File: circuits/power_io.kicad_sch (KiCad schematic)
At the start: 19 parts, among them J3 AD7606 out, J4 LASER+MPD out, J5 LASER PSU, J6 EXT 5V

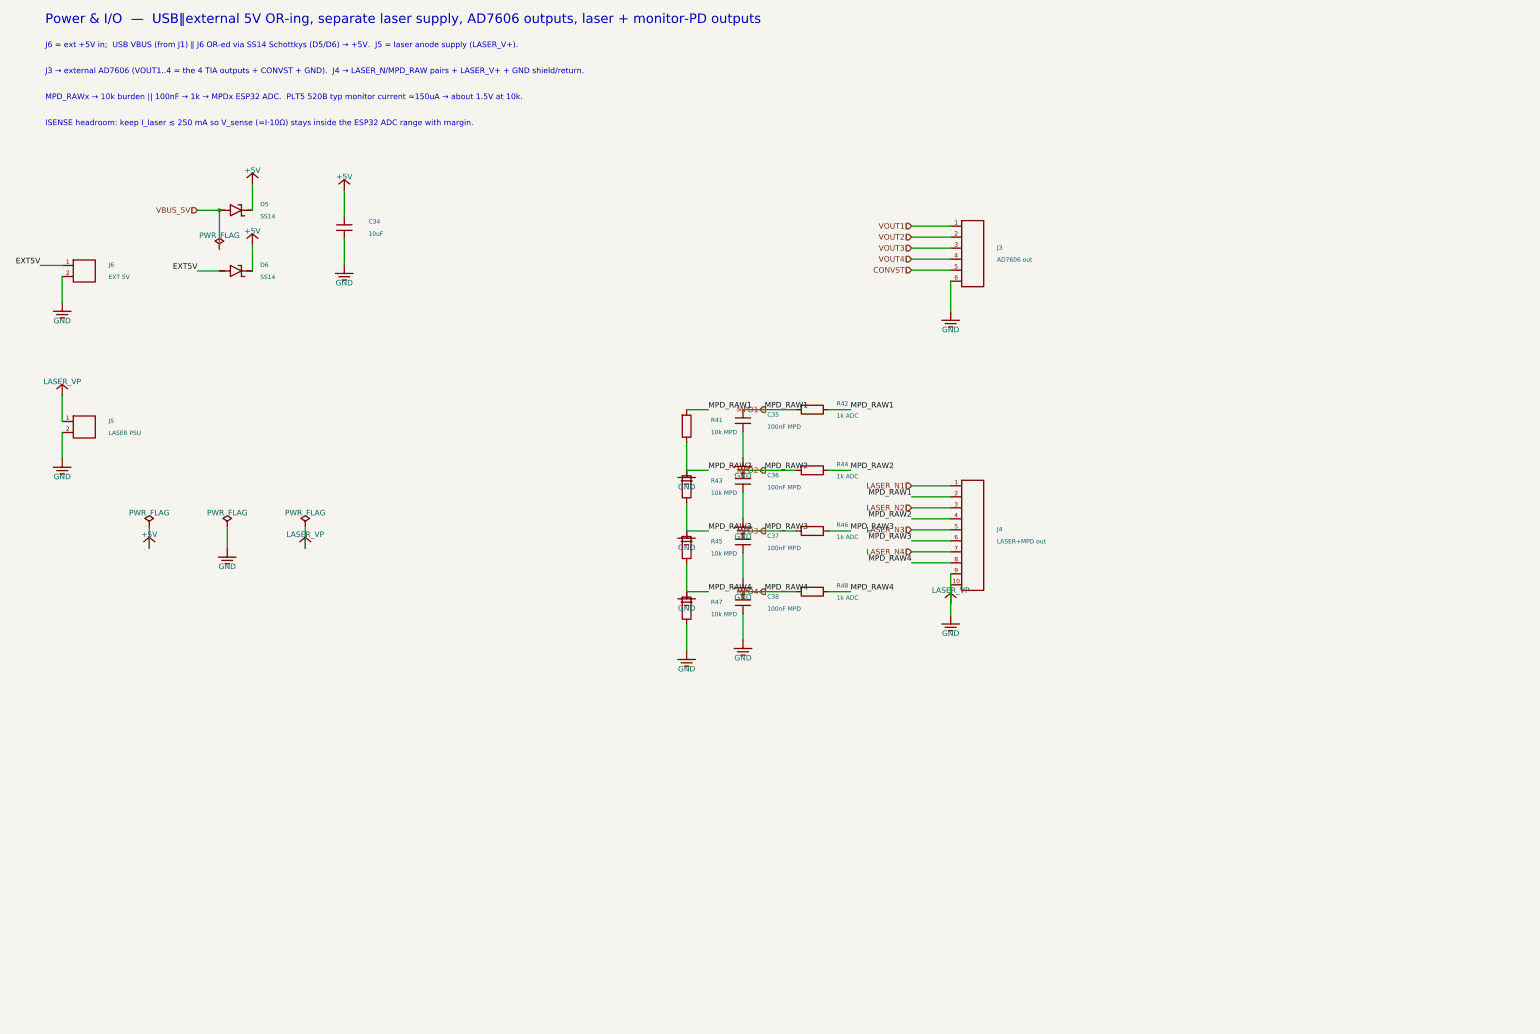
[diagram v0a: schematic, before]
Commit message: chore(circuits): update laser controller release artifacts
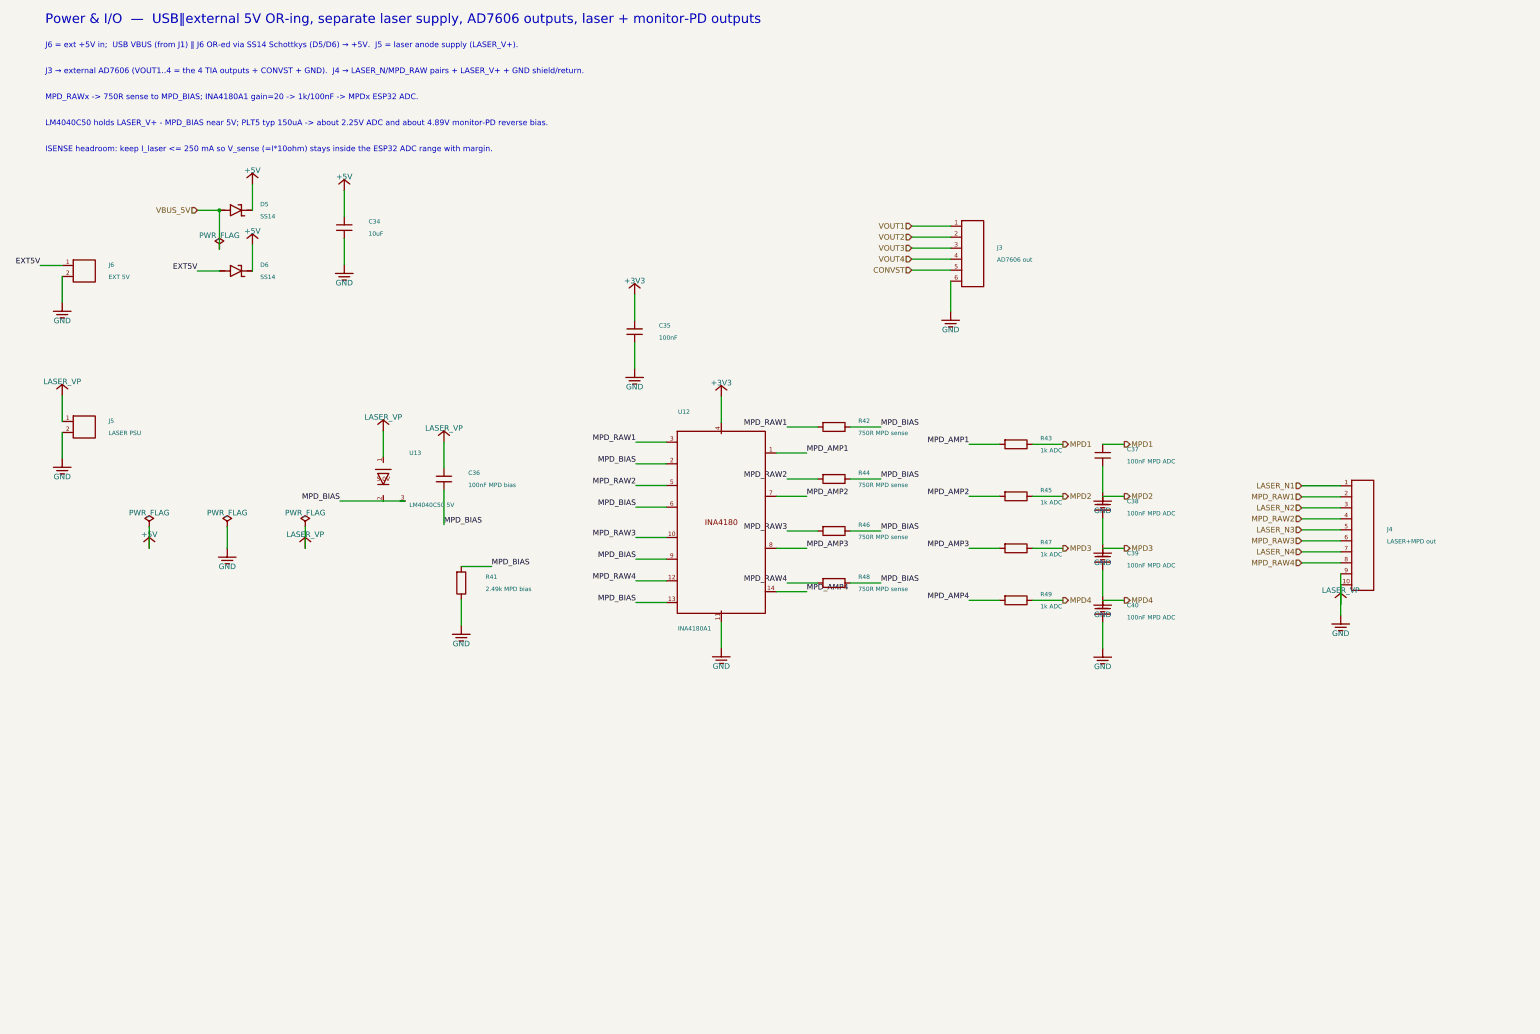
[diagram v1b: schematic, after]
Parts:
- removed C34: 10uF, Capacitor_SMD:C_0805_2012Metric_Pad1.18x1.45mm_HandSolder, symbol viv:C_V
- removed D5, D6: SS14, Diode_SMD:D_SMA, symbol viv:SCHOTTKY
- removed J3: AD7606 out, Connector_PinHeader_2.54mm:PinHeader_1x06_P2.54mm_Vertical, symbol viv:CONN6
- removed J5: LASER PSU, Connector_PinHeader_2.54mm:PinHeader_1x02_P2.54mm_Vertical, symbol viv:CONN2
- removed J6: EXT 5V, Connector_PinHeader_2.54mm:PinHeader_1x02_P2.54mm_Vertical, symbol viv:CONN2
- removed R43: 10k MPD, Resistor_SMD:R_0603_1608Metric_Pad0.98x0.95mm_HandSolder, symbol viv:R_V
- added C37, C38, C39, C40: 100nF MPD ADC, Capacitor_SMD:C_0402_1005Metric_Pad0.74x0.62mm_HandSolder, symbol viv:C_V
- added R43, R45, R47, R49: 1k ADC, Resistor_SMD:R_0603_1608Metric_Pad0.98x0.95mm_HandSolder, symbol viv:R_H
- added R44, R46: 750R MPD sense, Resistor_SMD:R_0603_1608Metric_Pad0.98x0.95mm_HandSolder, symbol viv:R_H
- added U12: INA4180A1, Package_SO:TSSOP-14_4.4x5mm_P0.65mm, symbol viv:INA4180_TSSOP14
- added U13: LM4040C50 5V, Package_TO_SOT_SMD:SOT-23, symbol viv:LM4040_DBZ
- C34: renamed from R47; value 10k MPD -> 10uF; footprint Resistor_SMD:R_0603_1608Metric_Pad0.98x0.95mm_HandSolder -> Capacitor_SMD:C_0805_2012Metric_Pad1.18x1.45mm_HandSolder; symbol viv:R_V -> viv:C_V; LCSC C269701 -> C15850; Part Number 0603WAF1002T5E -> CL21A106KAYNNNE
- C35: value 100nF MPD -> 100nF
- C36: value 100nF MPD -> 100nF MPD bias
- D5: renamed from R44; value 1k ADC -> SS14; footprint Resistor_SMD:R_0603_1608Metric_Pad0.98x0.95mm_HandSolder -> Diode_SMD:D_SMA; symbol viv:R_H -> viv:SCHOTTKY; LCSC C21190 -> C2480; Part Number 0603WAF1001T5E -> SS14
- D6: renamed from R45; value 10k MPD -> SS14; footprint Resistor_SMD:R_0603_1608Metric_Pad0.98x0.95mm_HandSolder -> Diode_SMD:D_SMA; symbol viv:R_V -> viv:SCHOTTKY; LCSC C269701 -> C2480; Part Number 0603WAF1002T5E -> SS14
- J3: renamed from C38; value 100nF MPD -> AD7606 out; footprint Capacitor_SMD:C_0402_1005Metric_Pad0.74x0.62mm_HandSolder -> Connector_PinHeader_2.54mm:PinHeader_1x06_P2.54mm_Vertical; symbol viv:C_V -> viv:CONN6; LCSC C1525 -> (none); Part Number CL05B104KO5NNNC -> (none)
- J5: renamed from R46; value 1k ADC -> LASER PSU; footprint Resistor_SMD:R_0603_1608Metric_Pad0.98x0.95mm_HandSolder -> Connector_PinHeader_2.54mm:PinHeader_1x02_P2.54mm_Vertical; symbol viv:R_H -> viv:CONN2; LCSC C21190 -> (none); Part Number 0603WAF1001T5E -> (none)
- J6: renamed from C37; value 100nF MPD -> EXT 5V; footprint Capacitor_SMD:C_0402_1005Metric_Pad0.74x0.62mm_HandSolder -> Connector_PinHeader_2.54mm:PinHeader_1x02_P2.54mm_Vertical; symbol viv:C_V -> viv:CONN2; LCSC C1525 -> (none); Part Number CL05B104KO5NNNC -> (none)
- R41: value 10k MPD -> 2.49k MPD bias; LCSC C269701 -> C22908; Part Number 0603WAF1002T5E -> 0603WAF2491T5E
- R42, R48: value 1k ADC -> 750R MPD sense; LCSC C21190 -> C114635; Part Number 0603WAF1001T5E -> RC0603FR-07750RL
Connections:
- net +5V: now also C34.1, D5.2 (K), D6.2 (K)
- net CONVST: now also J3.5
- net EXT5V: now also D6.1 (A), J6.1
- net GND: now also C36.1, J3.6, J5.1, J5.2, C37.2, C38.2, C39.2, C40.2, U12.11 (GND), U13.1 (K); no longer C36.2, D6.2, J3.2
- net MPD1: now also C37.1, R43.2; no longer R42.1
- net MPD2: now also C38.1, R45.2; no longer D5.1
- net MPD3: now also C39.1, R47.2; no longer J5.1
- net MPD4: now also C40.1, R49.2; no longer R48.1
- net MPD_RAW1: now also R42.1, U12.3 (IN+1); no longer C35.1, R41.1, R42.2
- net MPD_RAW2: now also R44.1, U12.5 (IN+2); no longer C36.1, D5.2
- net MPD_RAW3: now also R46.1, U12.10 (IN+3); no longer D6.1, J5.2, J6.1
- net MPD_RAW4: now also R48.1, U12.12 (IN+4); no longer C34.1, J3.1, R48.2
- net VBUS_5V: now also D5.1 (A)
- net VOUT1: now also J3.1
- net VOUT2: now also J3.2
- net VOUT3: now also J3.3
- net VOUT4: now also J3.4
- new net +3V3: C35.1, U12.4 (VS)
- new net MPD_AMP1: R43.1, U12.1 (OUT1)
- new net MPD_AMP2: R45.1, U12.7 (OUT2)
- new net MPD_AMP3: R47.1, U12.8 (OUT3)
- new net MPD_AMP4: R49.1, U12.14 (OUT4)
- new net MPD_BIAS: C36.2, R41.1, R42.2, R44.2, R46.2, R48.2, U12.13 (IN-4), U12.2 (IN-1), U12.6 (IN-2), U12.9 (IN-3), U13.2 (A), U13.3 (*)
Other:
- note added: "ISENSE headroom: keep I_laser <= 250 mA so V_sense (=I*10ohm) stays inside the ESP32 ADC range with margin."
- note added: "LM4040C50 holds LASER_V+ - MPD_BIAS near 5V; PLT5 typ 150uA -> about 2.25V ADC and about 4.89V monitor-PD reverse bias."
- note added: "MPD_RAWx -> 750R sense to MPD_BIAS; INA4180A1 gain=20 -> 1k/100nF -> MPDx ESP32 ADC."
- note removed: "ISENSE headroom: keep I_laser ≲ 250 mA so V_sense (=I·10Ω) stays inside the ESP32 ADC range with margin."
- note removed: "MPD_RAWx → 10k burden || 100nF → 1k → MPDx ESP32 ADC. PLT5 520B typ monitor current ≈150uA → about 1.5V at 10k."

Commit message: fix(circuits): import mcu sheet and laser footprints
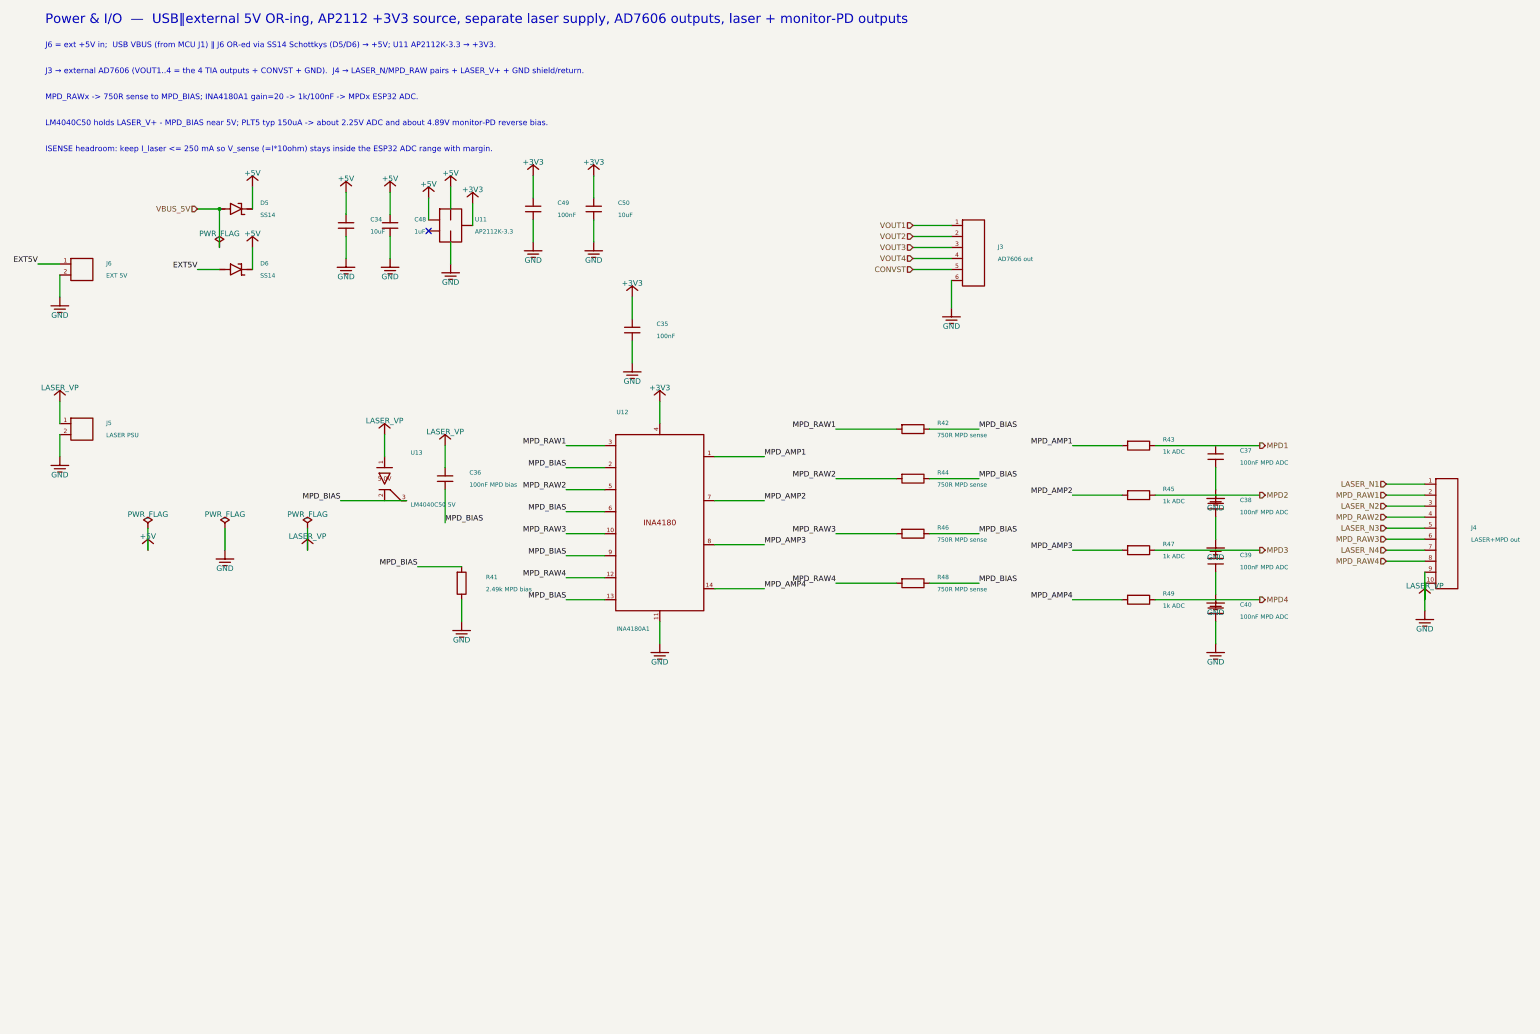
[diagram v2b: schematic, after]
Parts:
- added C48: 1uF, Capacitor_SMD:C_0402_1005Metric_Pad0.74x0.62mm_HandSolder, symbol viv:C_V
- added C49: 100nF, Capacitor_SMD:C_0402_1005Metric_Pad0.74x0.62mm_HandSolder, symbol viv:C_V
- added C50: 10uF, Capacitor_SMD:C_0805_2012Metric_Pad1.18x1.45mm_HandSolder, symbol viv:C_V
- added U11: AP2112K-3.3, Package_TO_SOT_SMD:SOT-23-5, symbol viv:LDO5
- C34: LCSC C15850 -> C318691; Part Number CL21A106KAYNNNE -> CL21A106KAYNNNG
- C35, C36, C37, C38, C39, C40: LCSC C1525 -> C83056; Part Number CL05B104KO5NNNC -> 0402B104K160CT
- R41: LCSC C22908 -> C2099849; Part Number 0603WAF2491T5E -> CRCW06032K49FKEAHP
- R43, R45, R47, R49: LCSC C21190 -> C2907002; Part Number 0603WAF1001T5E -> FRC0603F1001TS
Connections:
- net +3V3: now also C49.1, C50.1, U11.5 (VOUT)
- net +5V: now also C48.1, U11.1 (VIN), U11.3 (EN)
- net GND: now also C48.2, C49.2, C50.2, U11.2 (GND)
- no-connect marks 0 -> 1
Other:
- note added: "J6 = ext +5V in; USB VBUS (from MCU J1) ‖ J6 OR-ed via SS14 Schottkys (D5/D6) → +5V; U11 AP2112K-3.3 → +3V3."
- note added: "Power & I/O — USB‖external 5V OR-ing, AP2112 +3V3 source, separate laser supply, AD7606 outputs, laser + monitor-PD outputs"
- note removed: "J6 = ext +5V in; USB VBUS (from J1) ‖ J6 OR-ed via SS14 Schottkys (D5/D6) → +5V. J5 = laser anode supply (LASER_V+)."
- note removed: "Power & I/O — USB‖external 5V OR-ing, separate laser supply, AD7606 outputs, laser + monitor-PD outputs"

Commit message: save laser controller schematic and layout state
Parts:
- removed D5, D6: SS14, Diode_SMD:D_SMA, symbol viv:SCHOTTKY
- removed J5: LASER PSU, Connector_PinHeader_2.54mm:PinHeader_1x02_P2.54mm_Vertical, symbol viv:CONN2
- added C48: 1uF, Capacitor_SMD:C_0402_1005Metric_Pad0.74x0.62mm_HandSolder, symbol viv:C_V
- added C49: 100nF, Capacitor_SMD:C_0402_1005Metric_Pad0.74x0.62mm_HandSolder, symbol viv:C_V
- added C50: 10uF, Capacitor_SMD:C_0805_2012Metric_Pad1.18x1.45mm_HandSolder, symbol viv:C_V
- added C51, C52, C53, C54: 100nF ADC AVCC, Capacitor_SMD:C_0402_1005Metric_Pad0.74x0.62mm_HandSolder, symbol viv:C_V
- added C55: 100nF ADC VDRIVE, Capacitor_SMD:C_0402_1005Metric_Pad0.74x0.62mm_HandSolder, symbol viv:C_V
- added C56: 10uF ADC AVCC, Capacitor_SMD:C_0805_2012Metric_Pad1.18x1.45mm_HandSolder, symbol viv:C_V
- added C57, C58: 1uF ADC REGCAP, Capacitor_SMD:C_0402_1005Metric_Pad0.74x0.62mm_HandSolder, symbol viv:C_V
- added C59: 10uF ADC REF, Capacitor_SMD:C_0805_2012Metric_Pad1.18x1.45mm_HandSolder, symbol viv:C_V
- added C60: 10uF ADC REFCAP, Capacitor_SMD:C_0805_2012Metric_Pad1.18x1.45mm_HandSolder, symbol viv:C_V
- added U14: AD7606BSTZ-4, Package_QFP:LQFP-64_10x10mm_P0.5mm, symbol viv:AD7606_4
- C34: renamed from C49; value 100nF -> 10uF; footprint Capacitor_SMD:C_0402_1005Metric_Pad0.74x0.62mm_HandSolder -> Capacitor_SMD:C_0805_2012Metric_Pad1.18x1.45mm_HandSolder; LCSC C83056 -> C318691; Part Number 0402B104K160CT -> CL21A106KAYNNNG
- D5: renamed from C34; value 10uF -> SS14; footprint Capacitor_SMD:C_0805_2012Metric_Pad1.18x1.45mm_HandSolder -> Diode_SMD:D_SMA; symbol viv:C_V -> viv:SCHOTTKY; LCSC C318691 -> C2480; Part Number CL21A106KAYNNNG -> SS14
- D6: renamed from U11; value AP2112K-3.3 -> SS14; footprint Package_TO_SOT_SMD:SOT-23-5 -> Diode_SMD:D_SMA; symbol viv:LDO5 -> viv:SCHOTTKY; LCSC C51118 -> C2480; Part Number AP2112K-3.3TRG1 -> SS14
- J3: value AD7606 out -> ADC debug
- J5: renamed from C48; value 1uF -> LASER PSU; footprint Capacitor_SMD:C_0402_1005Metric_Pad0.74x0.62mm_HandSolder -> Connector_PinHeader_2.54mm:PinHeader_1x02_P2.54mm_Vertical; symbol viv:C_V -> viv:CONN2; LCSC C7472946 -> (none); Part Number HGC0402R5105K250NTEJ -> (none)
- U11: renamed from C50; value 10uF -> AP2112K-3.3; footprint Capacitor_SMD:C_0805_2012Metric_Pad1.18x1.45mm_HandSolder -> Package_TO_SOT_SMD:SOT-23-5; symbol viv:C_V -> viv:LDO5; LCSC C318691 -> C51118; Part Number CL21A106KAYNNNG -> AP2112K-3.3TRG1
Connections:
- net +3V3: now also U11.5 (VOUT), C49.1, C50.1, C55.1, U14.23 (VDRIVE), U14.34 (REF SELECT), U14.6 (PAR/SER/BYTE SEL), U14.7 (STBY); no longer C34.1, D6.5 (VOUT), U11.1
- net +5V: now also C34.1, D5.2 (K), D6.2 (K), U11.1 (VIN), U11.3 (EN), C48.1, C51.1, C52.1, C53.1, C54.1, C56.1, U14.1 (AVCC), U14.37 (AVCC), U14.38 (AVCC), U14.48 (AVCC); no longer D5.1, D6.1 (VIN), D6.3 (EN), J5.1
- net CONVST: now also U14.10 (CONVSTB), U14.9 (CONVSTA)
- net EXT5V: now also D6.1 (A)
- net GND: now also J5.1, C48.2, C49.2, C50.2, C51.2, C52.2, C53.2, C54.2, C55.2, C56.2, C57.2, C58.2, C59.2, C60.2, U14.16 (DB0), U14.17 (DB1), U14.18 (DB2), U14.19 (DB3), U14.2 (AGND), U14.20 (DB4), U14.21 (DB5), U14.22 (DB6), U14.26 (AGND), U14.27 (DB9), U14.28 (DB10), U14.29 (DB11), U14.3 (OS0), U14.30 (DB12), U14.31 (DB13), U14.32 (DB14/HBEN), U14.33 (DB15/BYTE SEL), U14.35 (AGND), U14.4 (OS1), U14.40 (AGND), U14.41 (AGND), U14.43 (REFGND), U14.46 (REFGND), U14.47 (AGND), U14.5 (OS2), U14.50 (V1GND), U14.52 (V2GND), U14.53 (AGND), U14.54 (AGND), U14.55 (AGND), U14.56 (AGND), U14.58 (V3GND), U14.60 (V4GND), U14.61 (AGND), U14.62 (AGND), U14.63 (AGND), U14.64 (AGND), U14.8 (RANGE); no longer D5.2, D6.2 (GND)
- net VBUS_5V: now also D5.1 (A)
- net VOUT1: now also U14.49 (V1)
- net VOUT2: now also U14.51 (V2)
- net VOUT3: now also U14.57 (V3)
- net VOUT4: now also U14.59 (V4)
- new net: C57.1, U14.36 (REGCAP)
- new net: C58.1, U14.39 (REGCAP)
- new net: C59.1, U14.42 (REFIN/REFOUT)
- new net: C60.1, U14.44 (REFCAPA), U14.45 (REFCAPB)
- new net ADC_BUSY: U14.14 (BUSY)
- new net ADC_CS: U14.13 (CS)
- new net ADC_MISO_A: U14.24 (DB7/DOUTA)
- new net ADC_MISO_B: U14.25 (DB8/DOUTB)
- new net ADC_RESET: U14.11 (RESET)
- new net ADC_SCLK: U14.12 (RD/SCLK)
- no-connect marks 1 -> 2
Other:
- note added: "Power & I/O — USB‖external 5V OR-ing, AP2112 +3V3 source, separate laser supply, on-board AD7606-4 ADC, laser + monitor-PD outputs"
- note added: "U14 AD7606BSTZ-4 digitizes VOUT1..4 on-board; ESP32 drives CONVST/SCLK/CS/RESET and reads BUSY + DOUTA/DOUTB. J3 is debug only."
- note removed: "J3 → external AD7606 (VOUT1..4 = the 4 TIA outputs + CONVST + GND). J4 → LASER_N/MPD_RAW pairs + LASER_V+ + GND shield/return."
- note removed: "Power & I/O — USB‖external 5V OR-ing, AP2112 +3V3 source, separate laser supply, AD7606 outputs, laser + monitor-PD outputs"
- moved on the sheet: C34
